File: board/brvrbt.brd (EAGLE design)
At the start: 160 x 100 mm, 9 parts

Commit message: layout
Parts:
- R1, R2: device adafruit:0207/12 -> adafruit:0207/7
- moved EYE2 55.4 mm to (5.08, 7.62), turned to 0 degrees
- moved R2 55.2 mm to (3.43, 16.5), turned to 270 degrees
- moved EYE1 40.3 mm to (49.5, 7.62), turned to 180 degrees
- moved R1 38.8 mm to (51.2, 16.5), turned to 270 degrees
- moved LEG2 33.6 mm to (16.5, 8.89), turned to 90 degrees
- moved NPN_2 31.8 mm to (15.2, 17.8), turned to 90 degrees
- moved LEG1 23.3 mm to (39.4, 8.89), turned to 90 degrees
- moved NPN_1 14.0 mm to (38.1, 17.8), turned to 90 degrees
- moved BATTERY 9.92 mm to (27.9, 8.89), turned to 90 degrees
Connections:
- net AGND renamed GND
- net N$1 renamed BASE_2
- net N$2 renamed COLLECTOR_2
- net N$3 renamed BASE_1
- net N$4 renamed COLLECTOR_1
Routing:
- net GND: track 0.00 -> 56.2 mm
- net VCC: track 0.00 -> 41.4 mm
- net BASE_1: track 0.00 -> 20.3 mm
- net BASE_2: track 0.00 -> 19.0 mm
- net COLLECTOR_2: track 0.00 -> 5.08 mm
- net COLLECTOR_1: track 0.00 -> 5.08 mm
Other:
- board size 160 x 100 mm -> 55.9 x 23.8 mm
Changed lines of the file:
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@@
 <board>
 <plain>
-<wire x1="0" y1="0" x2="160" y2="0" width="0" layer="20"/>
-<wire x1="160" y1="0" x2="160" y2="100" width="0" layer="20"/>
-<wire x1="160" y1="100" x2="0" y2="100" width="0" layer="20"/>
-<wire x1="0" y1="100" x2="0" y2="0" width="0" layer="20"/>
-<text x="11.43" y="36.83" size="1.778" layer="21">brvrbt</text>
+<wire x1="0" y1="0" x2="55.86" y2="0" width="0" layer="20"/>
+<wire x1="55.86" y1="0" x2="55.86" y2="23.8" width="0" layer="20"/>
+<wire x1="55.86" y1="23.8" x2="0" y2="23.8" width="0" layer="20"/>
+<wire x1="0" y1="23.8" x2="0" y2="0" width="0" layer="20"/>
+<text x="33.02" y="21.59" size="1.778" layer="21" rot="R180">brvrbt</text>
 </plain>
 <attributes>
@@
 </autorouter>
 <elements>
-<element name="R1" library="adafruit" package="0207/12" value="300Ω" x="12.7" y="11.43" smashed="yes" rot="R90">
-<attribute name="NAME" x="11.303" y="8.255" size="1.27" layer="25" ratio="10" rot="R90"/>
-<attribute name="VALUE" x="13.3858" y="9.144" size="1.27" layer="27" ratio="10" rot="R90"/>
-</element>
-<element name="NPN_1" library="transistor" library_urn="urn:adsk.eagle:library:402" package="TO92-EBC" value="" x="24.13" y="17.78" smashed="yes" rot="R270">
-<attribute name="NAME" x="25.908" y="20.32" size="1.27" layer="25" ratio="10" rot="R270"/>
-<attribute name="VALUE" x="19.558" y="20.32" size="1.27" layer="27" ratio="10" rot="R270"/>
-</element>
-<element name="EYE1" library="photo-elements" library_urn="urn:adsk.eagle:library:323" package="T0-46-A10XX" value="A1050_09" x="13.97" y="26.67" smashed="yes">
-<attribute name="NAME" x="10.795" y="30.48" size="1.27" layer="25"/>
-</element>
-<element name="LEG1" library="microbuilder" package="1X02_OVAL" value="" x="22.86" y="25.4" rot="R270"/>
-<element name="BATTERY" library="microbuilder" package="1X02_OVAL" value="" x="34.29" y="16.51" rot="R270"/>
-<element name="R2" library="adafruit" package="0207/12" value="300Ω" x="58.42" y="11.43" smashed="yes" rot="R90">
-<attribute name="NAME" x="57.023" y="8.255" size="1.27" layer="25" ratio="10" rot="R90"/>
-<attribute name="VALUE" x="59.1058" y="9.144" size="1.27" layer="27" ratio="10" rot="R90"/>
-</element>
-<element name="NPN_2" library="transistor" library_urn="urn:adsk.eagle:library:402" package="TO92-EBC" value="" x="46.99" y="17.78" smashed="yes" rot="R270">
-<attribute name="NAME" x="48.768" y="20.32" size="1.27" layer="25" ratio="10" rot="R270"/>
-<attribute name="VALUE" x="42.418" y="20.32" size="1.27" layer="27" ratio="10" rot="R270"/>
-</element>
-<element name="EYE2" library="photo-elements" library_urn="urn:adsk.eagle:library:323" package="T0-46-A10XX" value="A1050_09" x="57.15" y="26.67" smashed="yes" rot="R180">
-<attribute name="NAME" x="59.055" y="31.75" size="1.27" layer="25" rot="R180"/>
-</element>
-<element name="LEG2" library="microbuilder" package="1X02_OVAL" value="" x="45.72" y="25.4" rot="R270"/>
+<element name="R1" library="adafruit" package="0207/7" value="300Ω" x="51.181" y="16.51" smashed="yes" rot="R270">
+<attribute name="VALUE" x="50.4952" y="18.796" size="1.27" layer="27" ratio="10" rot="R270"/>
+</element>
+<element name="NPN_1" library="transistor" library_urn="urn:adsk.eagle:library:402" package="TO92-EBC" value="" x="38.1" y="17.78" smashed="yes" rot="R90">
+<attribute name="NAME" x="36.321996875" y="12.699996875" size="1.27" layer="25" ratio="10" rot="R90"/>
+<attribute name="VALUE" x="42.672" y="15.24" size="1.27" layer="27" ratio="10" rot="R90"/>
+</element>
+<element name="EYE1" library="photo-elements" library_urn="urn:adsk.eagle:library:323" package="T0-46-A10XX" value="A1050_09" x="49.53" y="7.62" smashed="yes" rot="R180">
+<attribute name="NAME" x="52.705" y="3.81" size="1.27" layer="25" rot="R180"/>
+</element>
+<element name="LEG1" library="microbuilder" package="1X02_OVAL" value="" x="39.37" y="8.89" smashed="yes" rot="R90">
+<attribute name="NAME" x="41.9862" y="5.7912" size="0.8128" layer="25" ratio="18" rot="R180"/>
+<attribute name="VALUE" x="42.545" y="6.35" size="0.4064" layer="27" ratio="10" rot="R90"/>
+</element>
+<element name="BATTERY" library="microbuilder" package="1X02_OVAL" value="" x="27.94" y="8.89" smashed="yes" rot="R90">
+<attribute name="NAME" x="30.5562" y="5.7912" size="0.8128" layer="25" ratio="18" rot="R180"/>
+<attribute name="VALUE" x="31.115" y="6.35" size="0.4064" layer="27" ratio="10" rot="R90"/>
+</element>
+<element name="R2" library="adafruit" package="0207/7" value="300Ω" x="3.429" y="16.51" smashed="yes" rot="R270">
+<attribute name="VALUE" x="2.7432" y="18.796" size="1.27" layer="27" ratio="10" rot="R270"/>
+</element>
+<element name="NPN_2" library="transistor" library_urn="urn:adsk.eagle:library:402" package="TO92-EBC" value="" x="15.24" y="17.78" smashed="yes" rot="R90">
+<attribute name="NAME" x="18.288003125" y="17.78" size="1.27" layer="25" ratio="10" rot="R270"/>
+<attribute name="VALUE" x="19.812" y="15.24" size="1.27" layer="27" ratio="10" rot="R90"/>
+</element>
+<element name="EYE2" library="photo-elements" library_urn="urn:adsk.eagle:library:323" package="T0-46-A10XX" value="A1050_09" x="5.08" y="7.62" smashed="yes">
+<attribute name="NAME" x="3.175" y="2.54" size="1.27" layer="25"/>
+</element>
+<element name="LEG2" library="microbuilder" package="1X02_OVAL" value="" x="16.51" y="8.89" smashed="yes" rot="R90">
+<attribute name="NAME" x="19.1262" y="5.7912" size="0.8128" layer="25" ratio="18" rot="R180"/>
+<attribute name="VALUE" x="19.685" y="6.35" size="0.4064" layer="27" ratio="10" rot="R90"/>
+</element>
 </elements>
 <signals>
-<signal name="AGND">
+<signal name="GND">
 <contactref element="BATTERY" pad="2"/>
 <contactref element="R1" pad="1"/>
@@
 <contactref element="R2" pad="1"/>
 <contactref element="NPN_2" pad="C"/>
-<wire x1="45.72" y1="15.24" x2="58.42" y2="5.08" width="0" layer="19" extent="1-1"/>
-<wire x1="34.29" y1="15.24" x2="45.72" y2="15.24" width="0" layer="19" extent="1-1"/>
-<wire x1="22.86" y1="15.24" x2="34.29" y2="15.24" width="0" layer="19" extent="1-1"/>
-<wire x1="12.7" y1="5.08" x2="22.86" y2="15.24" width="0" layer="19" extent="1-1"/>
-</signal>
-<signal name="N$1">
+<wire x1="3.429" y1="20.32" x2="16.51" y2="20.32" width="0.6096" layer="1"/>
+<wire x1="51.181" y1="20.32" x2="39.37" y2="20.32" width="0.6096" layer="1"/>
+<wire x1="16.51" y1="20.32" x2="17.78" y2="20.32" width="0.6096" layer="1"/>
+<wire x1="27.94" y1="10.16" x2="17.78" y2="20.32" width="0.6096" layer="1" curve="90"/>
+<wire x1="39.37" y1="20.32" x2="38.1" y2="20.32" width="0.6096" layer="1"/>
+<wire x1="38.1" y1="20.32" x2="27.94" y2="10.16" width="0.6096" layer="1" curve="90"/>
+</signal>
+<signal name="BASE_2">
 <contactref element="R1" pad="2"/>
 <contactref element="EYE1" pad="1"/>
 <contactref element="NPN_1" pad="B"/>
-<wire x1="12.7" y1="17.78" x2="22.86" y2="17.78" width="0" layer="19" extent="1-1"/>
-<wire x1="12.27" y1="26.67" x2="12.7" y2="17.78" width="0" layer="19" extent="1-1"/>
+<wire x1="39.37" y1="17.78" x2="46.101" y2="17.78" width="0.6096" layer="1"/>
+<wire x1="46.101" y1="17.78" x2="51.181" y2="12.7" width="0.6096" layer="1"/>
+<wire x1="51.181" y1="12.7" x2="51.181" y2="7.669" width="0.6096" layer="1"/>
+<wire x1="51.181" y1="7.669" x2="51.23" y2="7.62" width="0.6096" layer="1"/>
 </signal>
 <signal name="VCC">
@@
 <contactref element="EYE2" pad="2"/>
 <contactref element="LEG2" pad="1"/>
-<wire x1="45.72" y1="26.67" x2="55.45" y2="26.67" width="0" layer="19" extent="1-1"/>
-<wire x1="34.29" y1="17.78" x2="45.72" y2="26.67" width="0" layer="19" extent="1-1"/>
-<wire x1="22.86" y1="26.67" x2="34.29" y2="17.78" width="0" layer="19" extent="1-1"/>
-<wire x1="15.67" y1="26.67" x2="22.86" y2="26.67" width="0" layer="19" extent="1-1"/>
-</signal>
-<signal name="N$2">
+<wire x1="47.83" y1="7.62" x2="39.37" y2="7.62" width="0.6096" layer="1"/>
+<wire x1="16.187025" y1="7.62" x2="6.78" y2="7.62" width="0.6096" layer="1"/>
+<wire x1="16.187025" y1="7.62" x2="16.51" y2="7.62" width="0.4064" layer="1"/>
+<wire x1="39.37" y1="7.62" x2="27.94" y2="7.62" width="0.6096" layer="1"/>
+<wire x1="27.94" y1="7.62" x2="16.187025" y2="7.62" width="0.6096" layer="1"/>
+</signal>
+<signal name="COLLECTOR_2">
 <contactref element="LEG1" pad="2"/>
 <contactref element="NPN_1" pad="E"/>
-<wire x1="22.86" y1="20.32" x2="22.86" y2="24.13" width="0" layer="19" extent="1-1"/>
-</signal>
-<signal name="N$3">
+<wire x1="39.37" y1="15.24" x2="39.37" y2="10.16" width="0.6096" layer="1"/>
+</signal>
+<signal name="BASE_1">
 <contactref element="R2" pad="2"/>
 <contactref element="EYE2" pad="1"/>
 <contactref element="NPN_2" pad="B"/>
-<wire x1="58.42" y1="17.78" x2="58.85" y2="26.67" width="0" layer="19" extent="1-1"/>
-<wire x1="45.72" y1="17.78" x2="58.42" y2="17.78" width="0" layer="19" extent="1-1"/>
-</signal>
-<signal name="N$4">
+<wire x1="16.51" y1="17.78" x2="8.509" y2="17.78" width="0.6096" layer="1"/>
+<wire x1="8.509" y1="17.78" x2="3.429" y2="12.7" width="0.6096" layer="1"/>
+<wire x1="3.429" y1="12.7" x2="3.429" y2="7.669" width="0.6096" layer="1"/>
+<wire x1="3.429" y1="7.669" x2="3.38" y2="7.62" width="0.6096" layer="1"/>
+</signal>
+<signal name="COLLECTOR_1">
 <contactref element="LEG2" pad="2"/>
 <contactref element="NPN_2" pad="E"/>
-<wire x1="45.72" y1="20.32" x2="45.72" y2="24.13" width="0" layer="19" extent="1-1"/>
+<wire x1="16.51" y1="10.16" x2="16.51" y2="15.24" width="0.6096" layer="1"/>
 </signal>
 </signals>

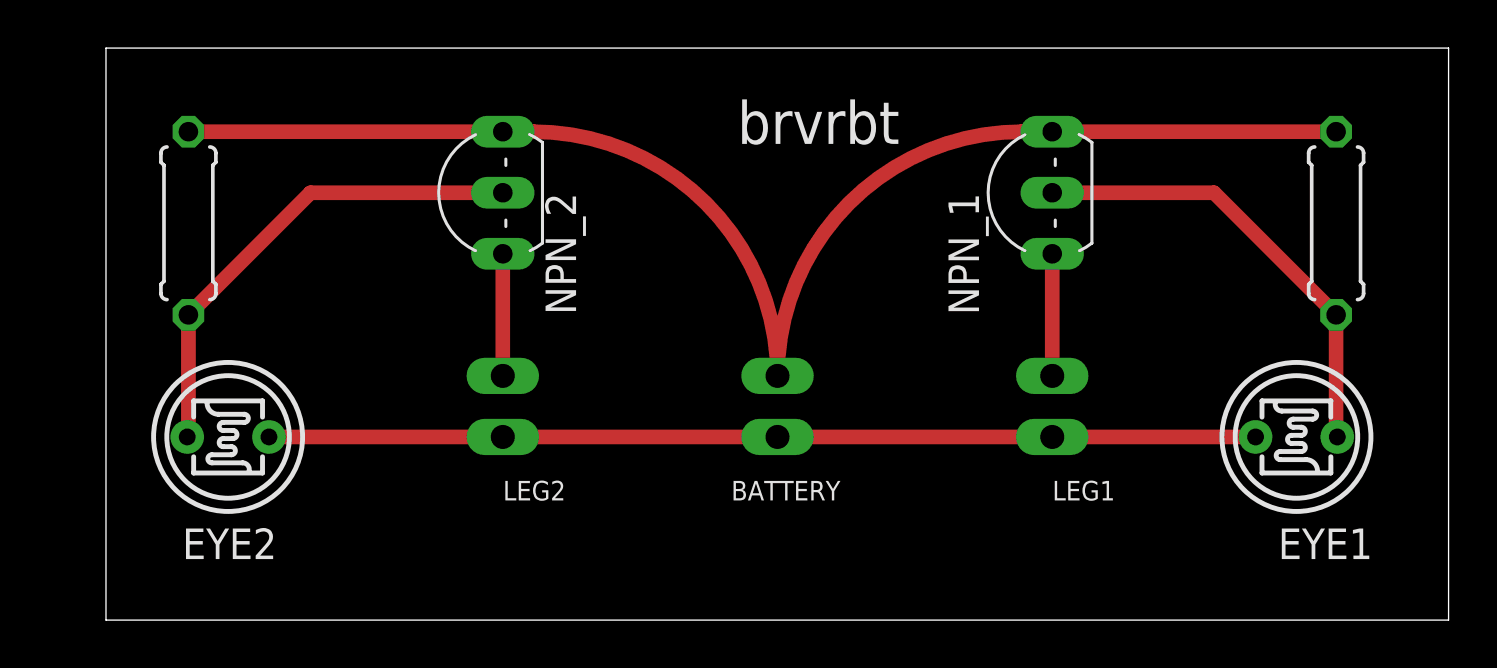
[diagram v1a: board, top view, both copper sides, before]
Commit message: small footprint 23x19mm
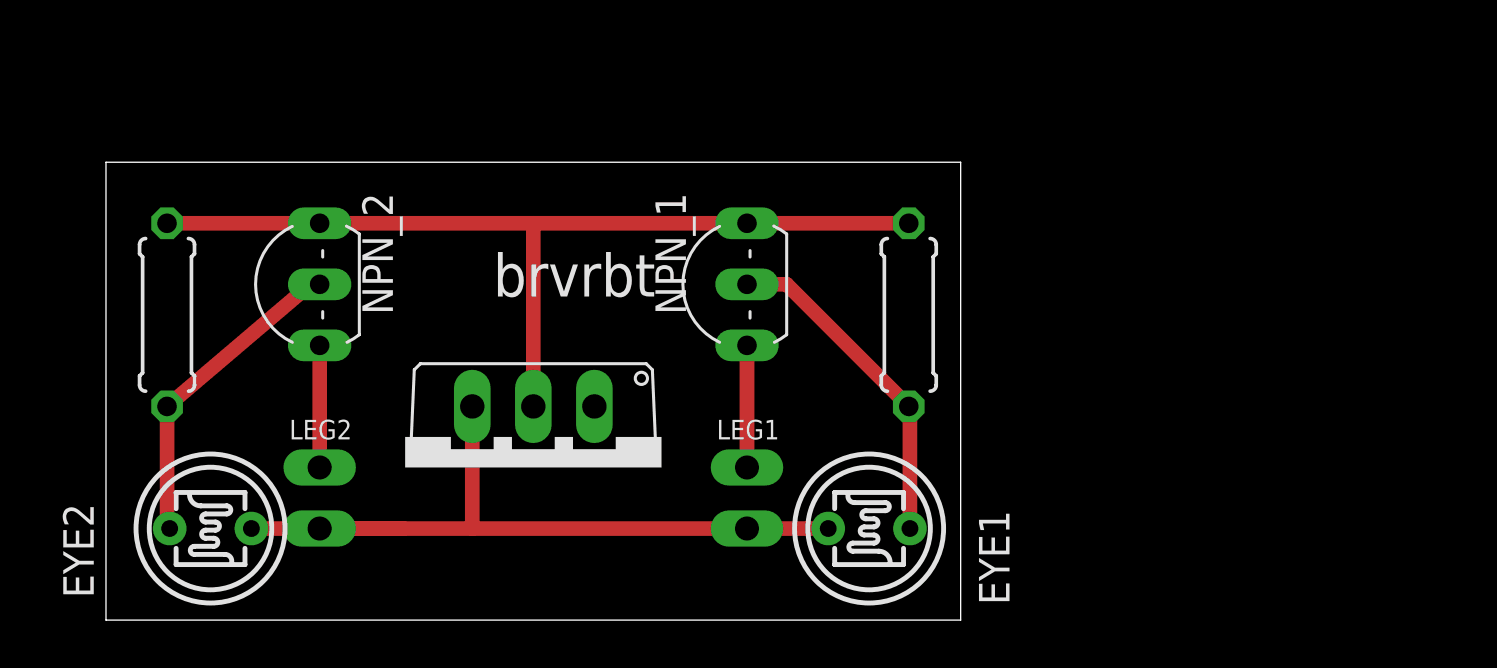
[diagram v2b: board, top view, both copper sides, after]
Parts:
- removed BATTERY: (no value), microbuilder:1X02_OVAL
- added IC1: 7805, linear:TO220V
- moved EYE1 18.2 mm to (31.8, 3.81)
- moved R1 18.2 mm to (33.4, 12.7)
- moved NPN_1 13.3 mm to (25.4, 14.0)
- moved LEG1 13.3 mm to (26.7, 5.08)
- moved LEG2 8.52 mm to (8.89, 5.08)
- moved NPN_2 8.52 mm to (7.62, 14.0)
- moved R2 3.91 mm to (2.54, 12.7)
- moved EYE2 3.88 mm to (4.35, 3.81)
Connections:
- removed net VCC: BATTERY.1, EYE1.2, EYE2.2, LEG1.1, LEG2.1
- new net 5V: EYE1.2, EYE2.2, IC1.3, LEG1.1, LEG2.1
- net GND: now also IC1.2; no longer BATTERY.2
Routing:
- net VCC: track 41.4 -> 0.00 mm
- net 5V: track 0.00 -> 36.1 mm
- net GND: track 56.2 -> 38.5 mm
- net BASE_1: track 20.3 -> 13.3 mm
- net BASE_2: track 19.0 -> 14.0 mm
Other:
- board size 55.9 x 23.8 mm -> 35.6 x 19.1 mm

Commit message: silk work
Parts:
- NPN_2: value (none) -> E B C
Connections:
- new net IN_BATT: IC1.1
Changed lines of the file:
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@@
 <attribute name="VALUE" x="1.8542" y="14.986" size="1.27" layer="27" ratio="10" rot="R270"/>
 </element>
-<element name="NPN_2" library="transistor" library_urn="urn:adsk.eagle:library:402" package="TO92-EBC" value="" x="7.62" y="13.97" smashed="yes" rot="R90">
+<element name="NPN_2" library="transistor" library_urn="urn:adsk.eagle:library:402" package="TO92-EBC" value="E B C" x="7.62" y="13.97" smashed="yes" rot="R90">
 <attribute name="NAME" x="10.668003125" y="17.78" size="1.27" layer="25" ratio="10" rot="R270"/>
 <attribute name="VALUE" x="12.192" y="11.43" size="1.27" layer="27" ratio="10" rot="R90"/>
@@
 <wire x1="15.24" y1="3.81" x2="8.89" y2="3.81" width="0.6096" layer="1"/>
 </signal>
+<signal name="IN_BATT">
+<contactref element="IC1" pad="1"/>
+</signal>
 </signals>
